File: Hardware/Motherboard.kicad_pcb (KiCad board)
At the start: 2 copper layers, 132.1 x 81.3 mm, 51 parts, among them J1 BME680, J2 JTAG, J3 Display_1, J4 Display_2, J5 Buttons, J6 USB, Q1 DMG3414U, SW1 Button_Plus, SW2 Button_Minus, SW3 Button_Settings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

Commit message: [Hardware] Displayed project date on PCB.
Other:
- board text added: "26/03/2020"
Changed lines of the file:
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@@
   (general
     (thickness 1.6)
-    (drawings 5)
+    (drawings 6)
     (tracks 463)
     (zones 0)
@@
     )
   )
+  (gr_text 26/03/2020 (at 146.05 15.24) (layer F.Mask)
+    (effects (font (size 1.5 1.5) (thickness 0.3)))
+  )
   (gr_text MCLR (at 124.46 54.61) (layer F.SilkS)

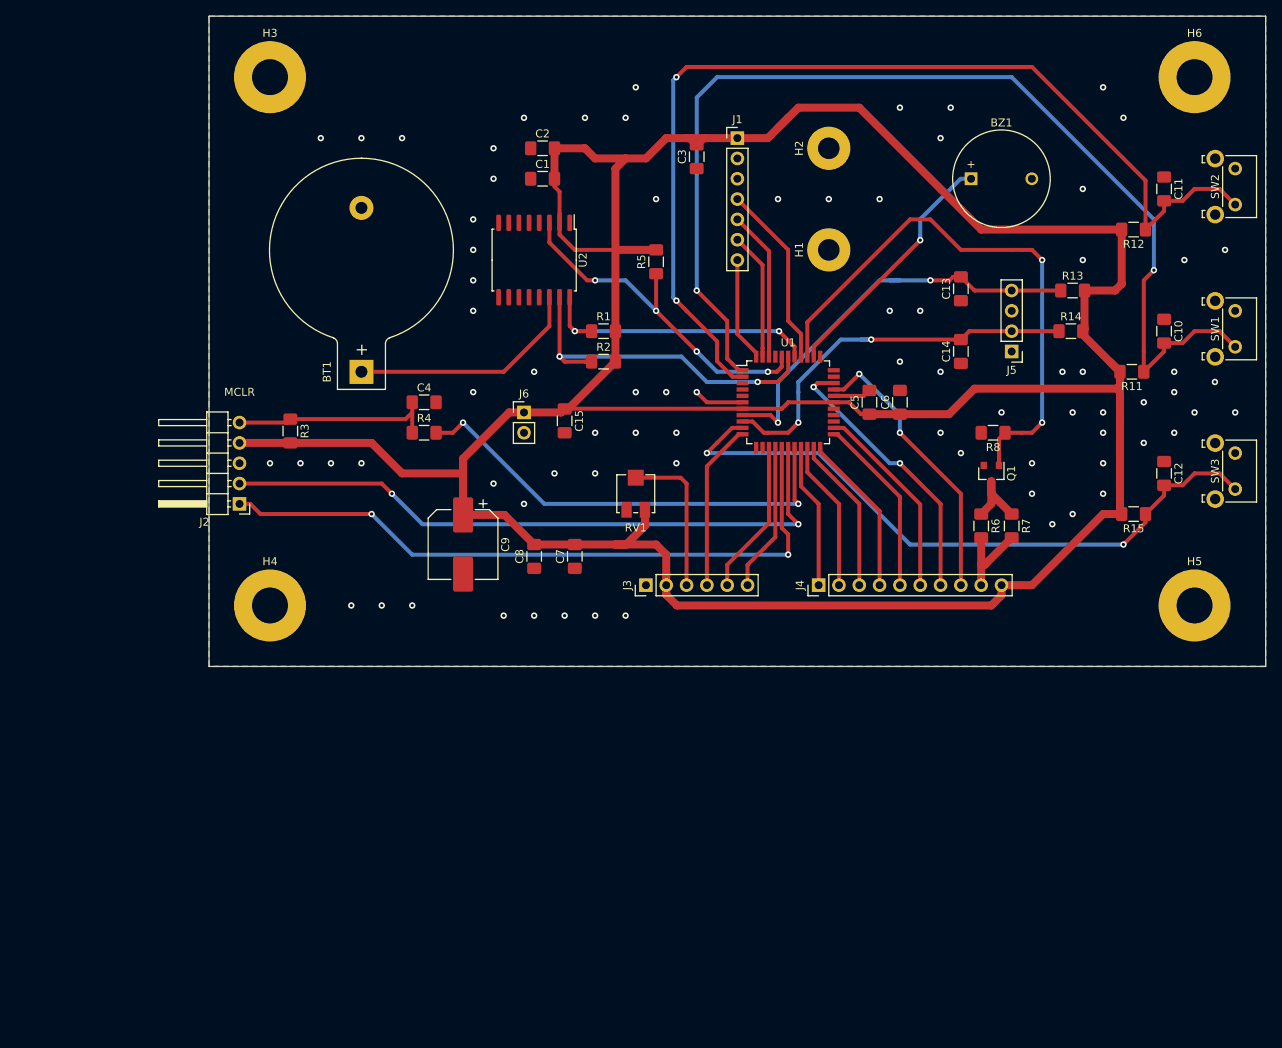
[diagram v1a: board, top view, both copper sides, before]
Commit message: [Hardware] Added alarm and backlight buttons parts to both schematic and PCB.
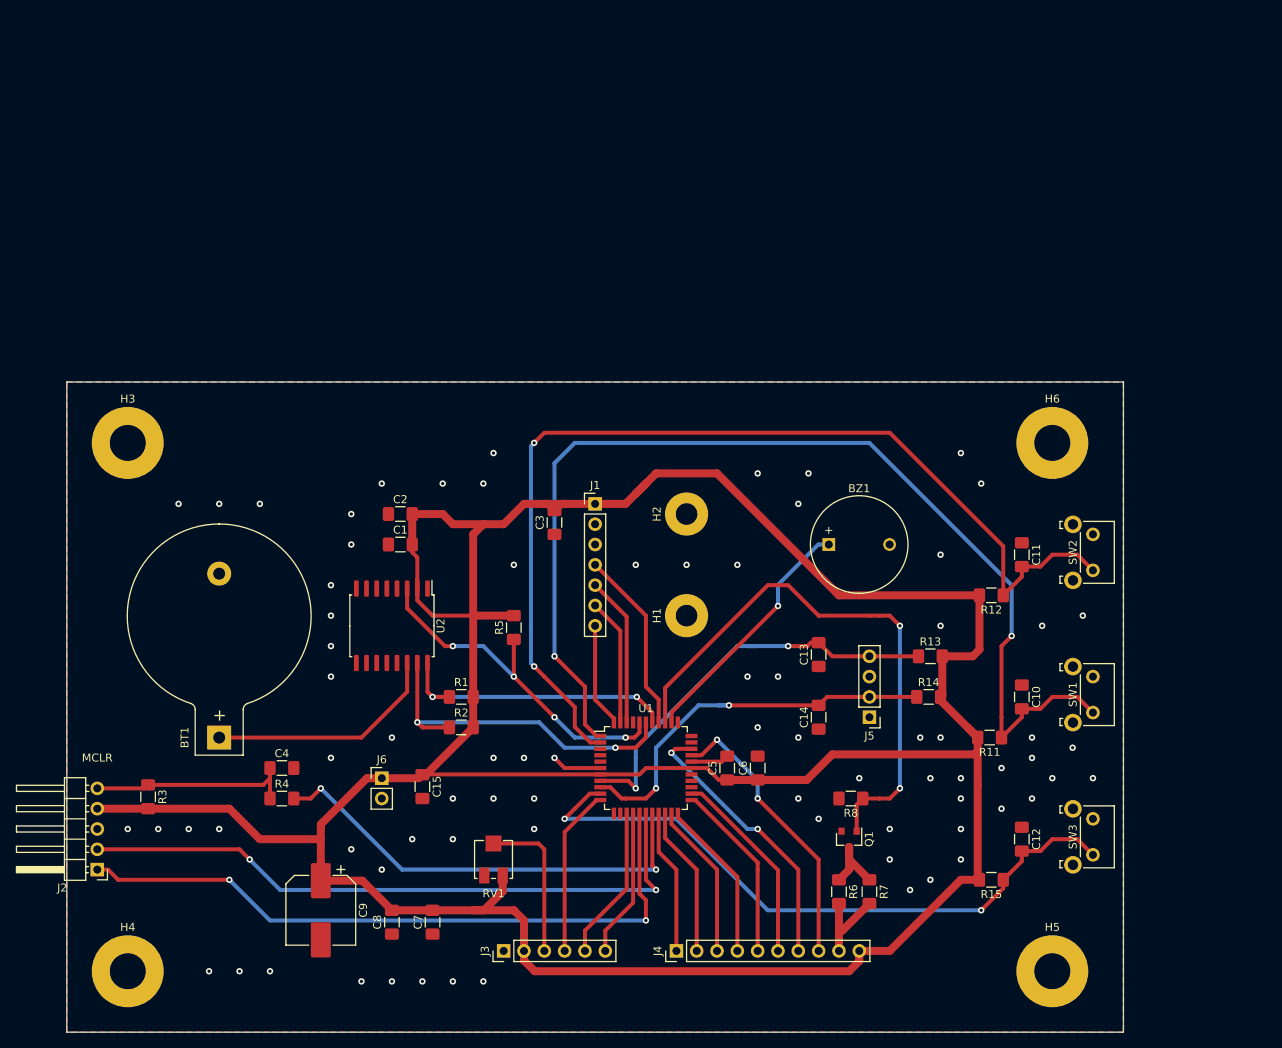
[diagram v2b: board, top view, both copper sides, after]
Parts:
- added SW4: Inverter_8013, Empty_Footprint:Empty_Footprint, F.Cu at (72.4, 100.3)
- added SW5: Push_Button_R1500, Empty_Footprint:Empty_Footprint, F.Cu at (72.4, 118.1)
- moved C7 49.1 mm to (148.6, 120.9)
- moved C8 49.1 mm to (143.5, 120.9)
- moved C11 49.1 mm to (222.2, 74.9)
- moved J6 49.1 mm to (142.2, 102.9)
- moved R11 49.1 mm to (218.2, 97.8)
- moved R12 49.1 mm to (218.4, 80.0)
- moved SW3 49.1 mm to (231.1, 108.0)
- moved BT1 49.1 mm to (121.9, 97.8)
- moved BZ1 49.1 mm to (198.1, 73.7)
- moved C1 49.1 mm to (144.6, 73.7)
- moved C12 49.1 mm to (222.2, 110.5)
- moved C14 49.1 mm to (196.8, 95.2)
- moved C15 49.1 mm to (147.3, 103.9)
- moved C2 49.1 mm to (144.6, 69.8)
- moved C3 49.1 mm to (163.8, 70.9)
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
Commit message: [Hardware] Added USB connector supply part to both schematic and PCB.
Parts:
- added J7: MUSBD111M0_Supply, Empty_Footprint:Empty_Footprint, F.Cu at (72.4, 128.3)
- moved SW4 7.62 mm to (72.4, 92.7)
- moved SW5 7.62 mm to (72.4, 110.5)
- moved U3 7.62 mm to (72.4, 57.1)
- moved U4 7.62 mm to (72.4, 74.9)
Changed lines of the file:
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@@
     (tracks 463)
     (zones 0)
-    (modules 53)
+    (modules 54)
     (nets 51)
   )
@@
   )
   (setup
-    (last_trace_width 1)
+    (last_trace_width 0.5)
     (user_trace_width 0.5)
     (user_trace_width 1)
@@
   )
   (module Empty_Footprint:Empty_Footprint (layer F.Cu)
-    (at 72.39 118.11)
-    (fp_text reference SW5 (at -3.81 6.35) (layer Eco1.User)
-      (effects (font (size 1 1) (thickness 0.15)))
-    )
-    (fp_text value Push_Button_R1500 (at 0 8.89) (layer Eco1.User)
+    (at 72.39 128.27)
+    (fp_text reference J7 (at -3.81 6.35) (layer Eco1.User)
+      (effects (font (size 1 1) (thickness 0.15)))
+    )
+    (fp_text value MUSBD111M0_Supply (at 0 8.89) (layer Eco1.User)
       (effects (font (size 1 1) (thickness 0.15)))
     )
@@
   )
   (module Empty_Footprint:Empty_Footprint (layer F.Cu)
-    (at 72.39 100.33)
+    (at 72.39 110.49)
+    (fp_text reference SW5 (at -3.81 6.35) (layer Eco1.User)
+      (effects (font (size 1 1) (thickness 0.15)))
+    )
+    (fp_text value Push_Button_R1500 (at 0 8.89) (layer Eco1.User)
+      (effects (font (size 1 1) (thickness 0.15)))
+    )
+    (fp_line (start 7.62 -3.81) (end -7.62 -3.81) (layer Eco1.User) (width 0.12))
+    (fp_line (start 7.62 5.08) (end 7.62 -3.81) (layer Eco1.User) (width 0.12))
+    (fp_line (start -7.62 5.08) (end 7.62 5.08) (layer Eco1.User) (width 0.12))
+    (fp_line (start -7.62 -3.81) (end -7.62 5.08) (layer Eco1.User) (width 0.12))
+  )
+  (module Empty_Footprint:Empty_Footprint (layer F.Cu)
+    (at 72.39 92.71)
     (fp_text reference SW4 (at -3.81 6.35) (layer Eco1.User)
       (effects (font (size 1 1) (thickness 0.15)))
@@
   )
   (module Empty_Footprint:Empty_Footprint (layer F.Cu)
-    (at 72.39 82.55)
+    (at 72.39 74.93)
     (fp_text reference U4 (at -3.81 6.35) (layer Eco1.User)
       (effects (font (size 1 1) (thickness 0.15)))
@@
   )
   (module Empty_Footprint:Empty_Footprint (layer F.Cu)
-    (at 72.39 64.77)
+    (at 72.39 57.15)
     (fp_text reference U3 (at -3.81 6.35) (layer Eco1.User)
       (effects (font (size 1 1) (thickness 0.15)))
@@
   (segment (start 128.27 101.6) (end 128.27 102.87) (width 0.5) (layer F.Cu) (net 18))
   (segment (start 128.27 102.87) (end 128.27 105.41) (width 0.5) (layer F.Cu) (net 18))
-  (segment (start 174.46 107.3) (end 174.46 117.31) (width 0.5) (layer F.Cu) (net 50))
-  (segment (start 174.46 117.31) (end 175.26 118.11) (width 0.5) (layer F.Cu) (net 50))
-  (segment (start 175.26 118.11) (end 175.26 118.11) (width 0.5) (layer F.Cu) (net 50))
-  (segment (start 175.26 107.3) (end 175.26 115.57) (width 0.5) (layer F.Cu) (net 49))
-  (segment (start 175.26 115.57) (end 176.53 116.84) (width 0.5) (layer F.Cu) (net 49))
-  (segment (start 176.53 116.84) (end 176.53 116.84) (width 0.5) (layer F.Cu) (net 49))
-  (segment (start 176.53 116.84) (end 176.53 116.84) (width 0.5) (layer F.Cu) (net 49))
   (segment (start 200.66 114.3) (end 199.39 115.57) (width 1) (layer F.Cu) (net 19))
   (segment (start 200.66 111.49) (end 200.66 114.3) (width 1) (layer F.Cu) (net 19))
@@
   (segment (start 160.890001 61.359999) (end 160.890001 88.500001) (width 0.5) (layer B.Cu) (net 48))
   (segment (start 161.29 60.96) (end 160.890001 61.359999) (width 0.5) (layer B.Cu) (net 48))
+  (segment (start 175.26 107.3) (end 175.26 115.57) (width 0.5) (layer F.Cu) (net 49))
+  (segment (start 175.26 115.57) (end 176.53 116.84) (width 0.5) (layer F.Cu) (net 49))
+  (segment (start 176.53 116.84) (end 176.53 116.84) (width 0.5) (layer F.Cu) (net 49))
+  (segment (start 176.53 116.84) (end 176.53 116.84) (width 0.5) (layer F.Cu) (net 49))
   (segment (start 106.68 111.76) (end 124.46 111.76) (width 0.5) (layer F.Cu) (net 49))
   (segment (start 124.46 111.76) (end 125.73 113.03) (width 0.5) (layer F.Cu) (net 49))
@@
   (via (at 125.73 113.03) (size 0.8) (drill 0.4) (layers F.Cu B.Cu) (net 49))
   (segment (start 173.99 116.84) (end 176.53 116.84) (width 0.5) (layer B.Cu) (net 49))
+  (segment (start 174.46 107.3) (end 174.46 117.31) (width 0.5) (layer F.Cu) (net 50))
+  (segment (start 174.46 117.31) (end 175.26 118.11) (width 0.5) (layer F.Cu) (net 50))
+  (segment (start 175.26 118.11) (end 175.26 118.11) (width 0.5) (layer F.Cu) (net 50))
   (segment (start 108.03 114.3) (end 109.3 115.57) (width 0.5) (layer F.Cu) (net 50))
   (segment (start 106.68 114.3) (end 108.03 114.3) (width 0.5) (layer F.Cu) (net 50))

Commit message: [Hardware] Renamed LCD display symbol for more coherency.
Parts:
- U4: value DEM20485SYH-LY -> DEM20485SYH-LY_Supply
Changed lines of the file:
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@@
       (effects (font (size 1 1) (thickness 0.15)))
     )
-    (fp_text value DEM20485SYH-LY (at 0 8.89) (layer Eco1.User)
+    (fp_text value DEM20485SYH-LY_Supply (at 0 8.89) (layer Eco1.User)
       (effects (font (size 1 1) (thickness 0.15)))
     )

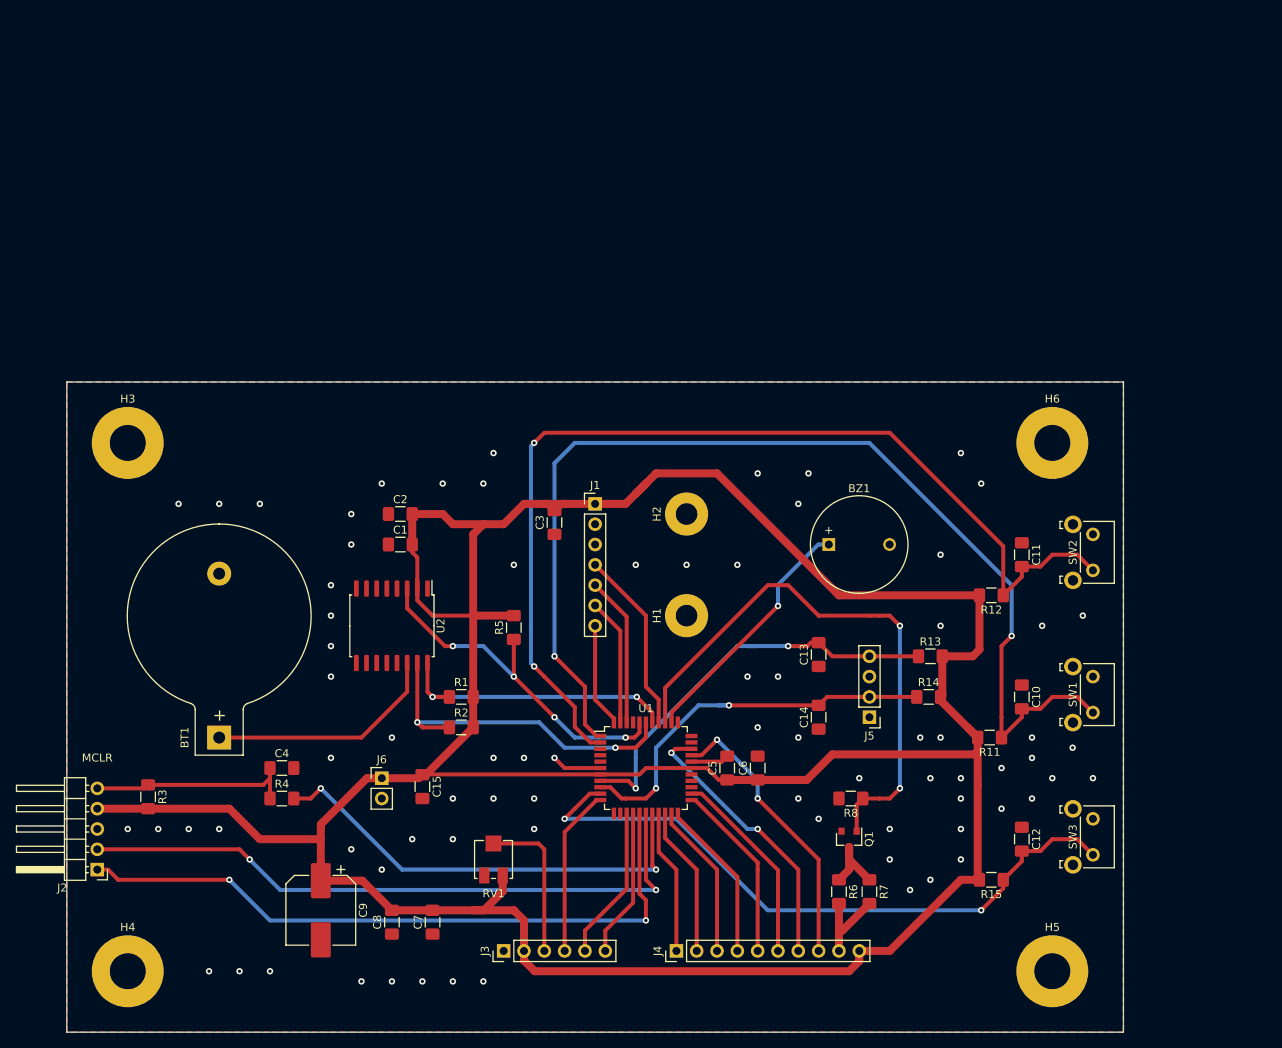
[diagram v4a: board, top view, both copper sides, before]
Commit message: [Hardware] Slightly decreased PCB width and adjusted it to millimeters.
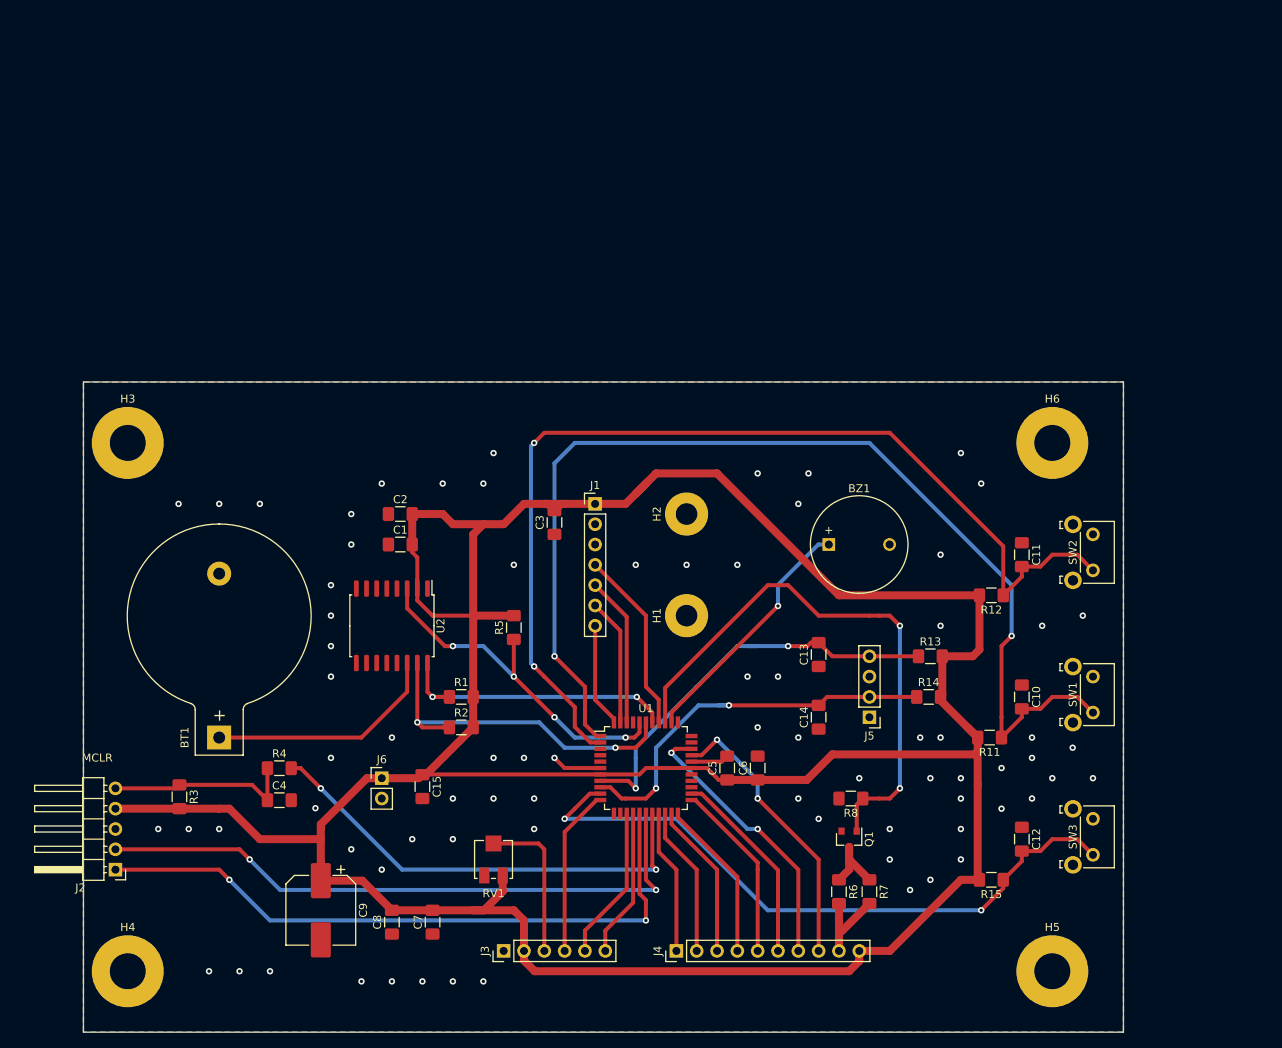
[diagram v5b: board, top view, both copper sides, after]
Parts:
- moved C4 4.03 mm to (129.4, 105.6)
- moved R3 3.92 mm to (117.0, 105.2)
- moved R4 3.80 mm to (129.4, 101.6)
- moved J2 2.27 mm to (109.0, 114.3)
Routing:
- net Net-(J2-Pad2): track 82.0 -> 79.8 mm
- net Net-(J2-Pad1): track 84.9 -> 82.6 mm
- net +5V: track 413.4 -> 411.2 mm
- net Net-(C4-Pad1): track 25.9 -> 24.0 mm
- net /RE3: track 57.2 -> 58.1 mm
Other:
- board size 132.1 x 81.3 mm -> 130 x 81.3 mm
